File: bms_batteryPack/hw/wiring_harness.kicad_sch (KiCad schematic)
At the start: 3 parts

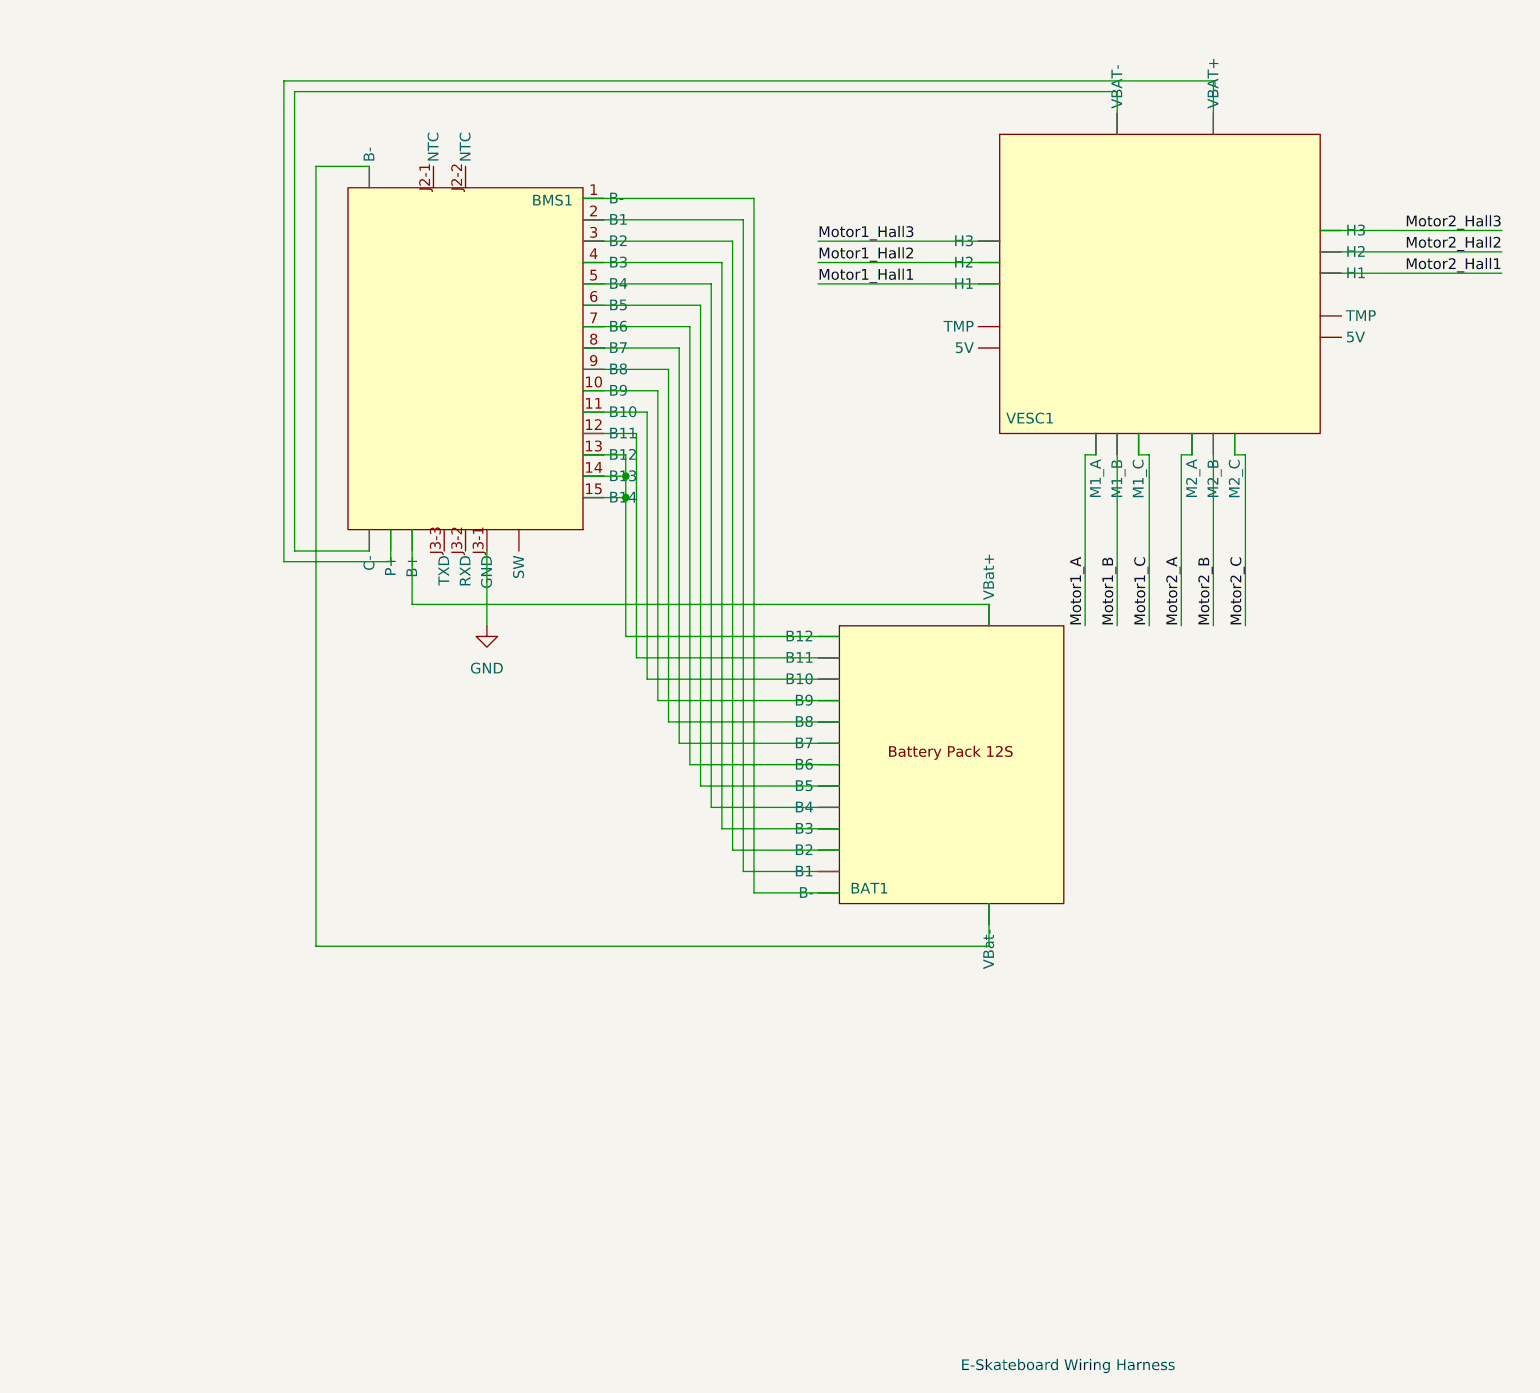
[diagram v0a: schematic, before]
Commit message: Added charger port and switch to wiring harness schematic
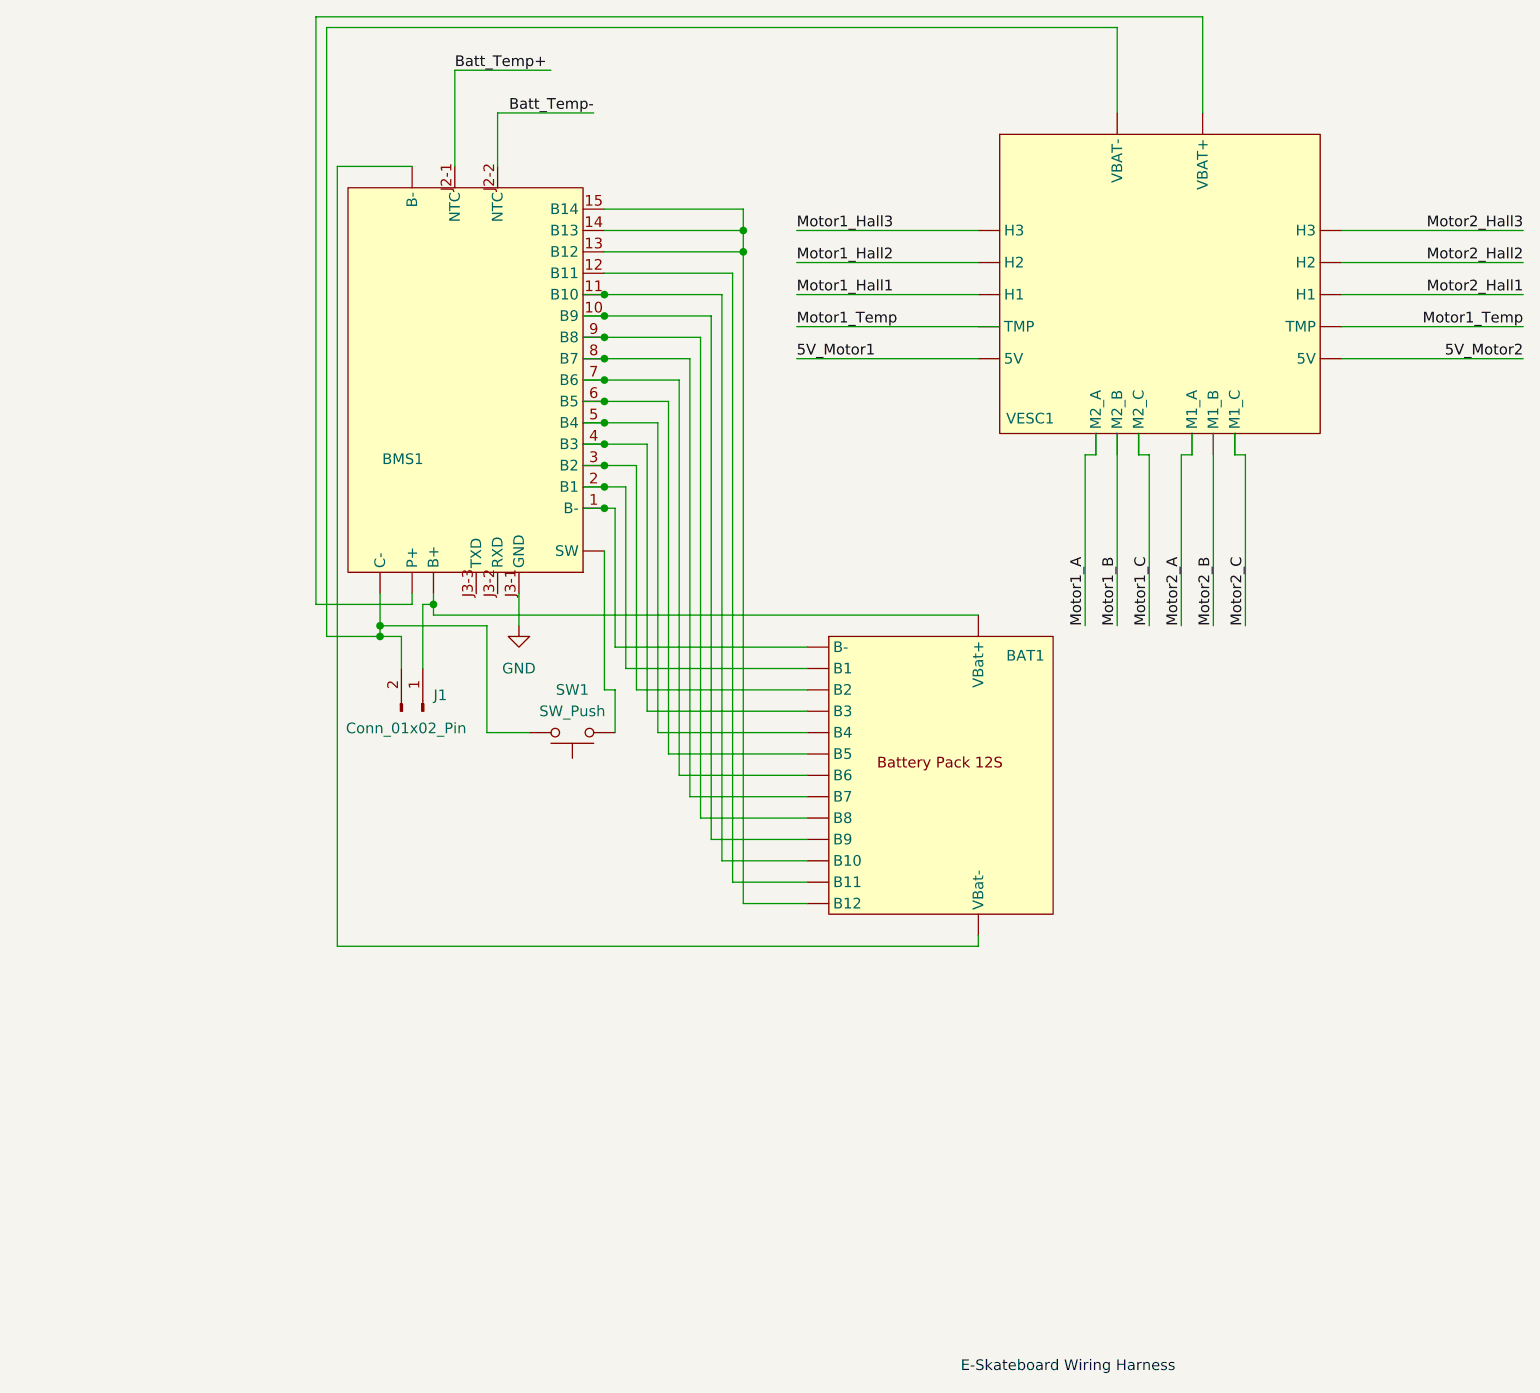
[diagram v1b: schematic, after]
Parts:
- added J1: Conn_01x02_Pin, symbol Connector:Conn_01x02_Pin
- added SW1: SW_Push, symbol Switch:SW_Push
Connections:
- net GND: now also BMS1.J3-1 (GND)
- net Motor1_B: no longer VESC1. (5V)
- net Motor2_B: no longer VESC1. (5V)
- net at BAT1. (VBat-): now also BMS1.9 (B8); no longer BMS1. (B-)
- net at BMS1. (C-): now also SW1.1; no longer BAT1. (VBat-)
- net Batt_Temp+: now reaches BMS1.J2-1 (NTC)
- net Batt_Temp-: now reaches BMS1.J2-2 (NTC)
- new net: BAT1. (VBat-), BMS1. (C-)
- new net: BAT1. (VBat-), BMS1. (C-), J1.1 (Pin_1)
- new net: BMS1. (C-), J1.2 (Pin_2), SW1.2, VESC1. (5V)
- new net: BMS1. (C-), VESC1. (5V)
- new net 5V_Motor1: VESC1. (5V)
- new net 5V_Motor2: VESC1. (5V)
- new net Motor1_Temp: VESC1. (5V)
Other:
- moved on the sheet: BAT1, BMS1, VESC1

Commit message: Updated with VESC receiver and button
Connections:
- net Motor1_A is gone; now on net Motor2_Hall3: VESC1. (5V)
- net Motor1_C is gone; now on net Motor2_Hall3: VESC1. (5V)
- net Motor2_A is gone; now on net Motor2_Hall3: VESC1. (5V)
- net Motor2_C is gone; now on net Motor2_Hall3: VESC1. (5V)
- net GND: now also VESC1. (5V)
- net at BAT1. (VBat-): now also BMS1.9 (B8); no longer BMS1. (C-)
- net at BMS1. (C-), J1.2 (Pin_2), VESC1. (5V): no longer SW1.2
- net at SW1.1: now also VESC1. (5V); no longer BMS1. (C-)
- new net: BAT1. (VBat-), BMS1. (C-)
- new net: BAT1. (VBat-), BMS1. (C-), J1.1 (Pin_1), VESC1. (5V)
- new net: SW1.2, VESC1. (5V)
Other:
- moved on the sheet: BAT1, J1, SW1, VESC1
